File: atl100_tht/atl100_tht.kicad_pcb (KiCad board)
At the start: 2 copper layers, 150 x 100 mm, 43 parts, among them J1 Conn_01x04_Pin, J2 Screw_Terminal_01x02, J3 Screw_Terminal_01x02, J4 Screw_Terminal_01x02, J5 Screw_Terminal_01x02, J6 Screw_Terminal_01x04, J7 Screw_Terminal_01x04, J8 Screw_Terminal_01x06, U2 ESP32-S3 DevKit, U3 HW-519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

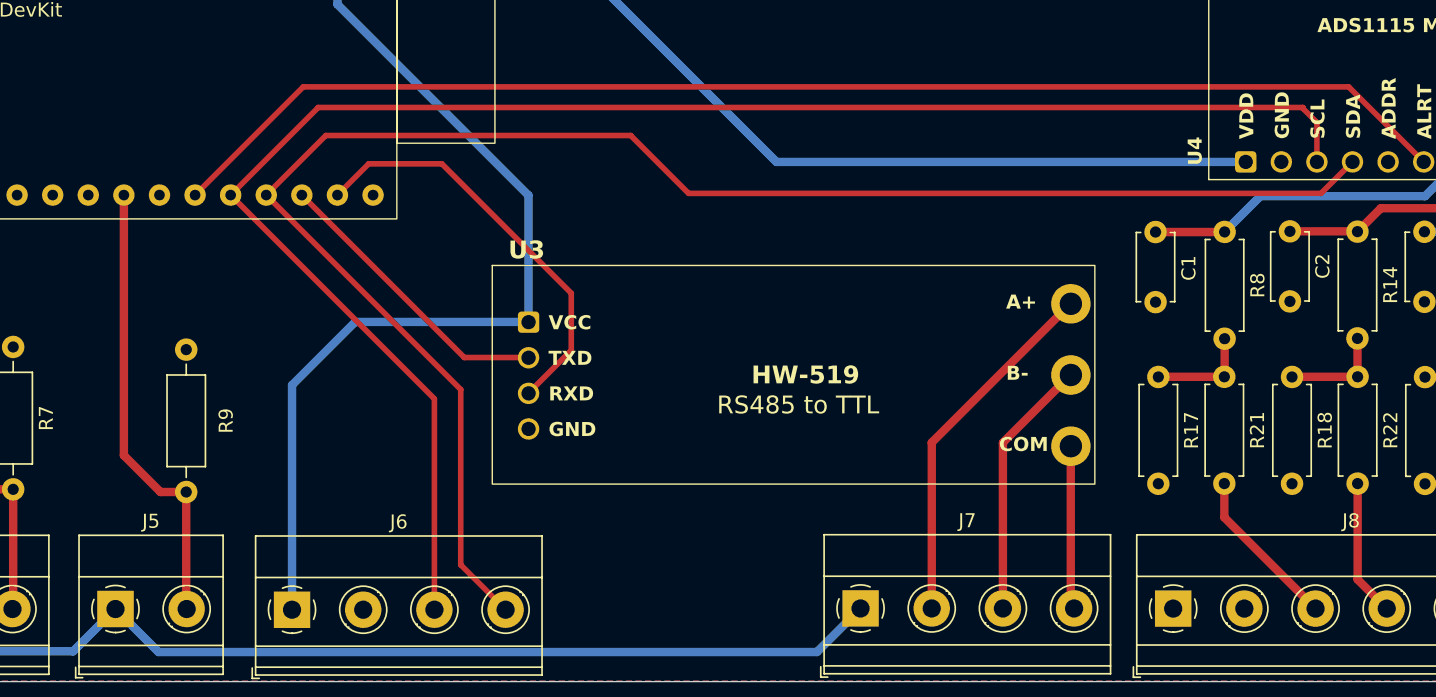
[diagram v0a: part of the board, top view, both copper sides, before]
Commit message: feat: Updated pins to RS-485 UART
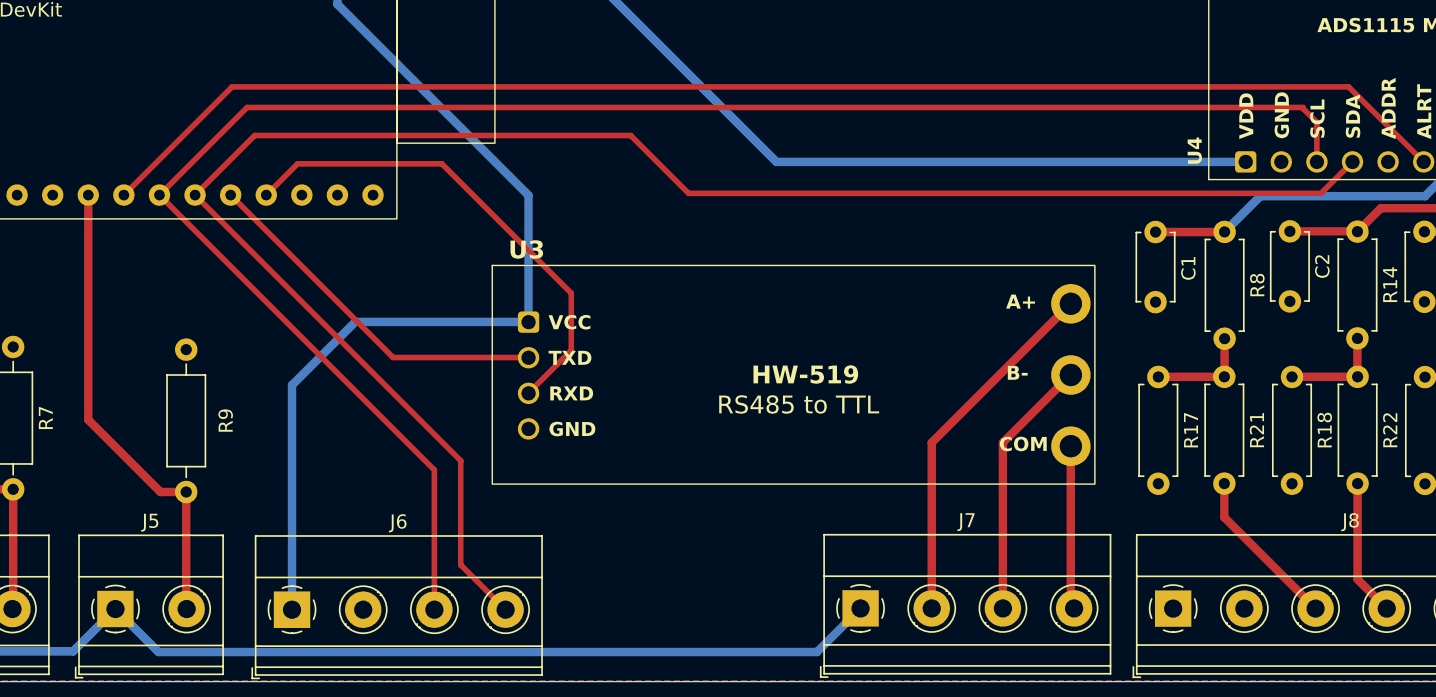
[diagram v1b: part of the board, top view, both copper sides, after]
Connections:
- U2 pad 24: MCU_TXD - RS485_RXD -> unconnected-(U2-U0TXD/GPIO43-Pad24)
- U2 pad 25: MCU_RXD - RS485_TXD -> unconnected-(U2-U0RXD/GPIO44-Pad25)
- U2 pad 26: I2C_SDA -> MCU_TXD - RS485_RXD
- U2 pad 27: I2C_SCL -> MCU_RXD - RS485_TXD
- U2 pad 28: ADC_ALERT -> I2C_SDA
- U2 pad 29: unconnected-(U2-MTDI/GPIO41-Pad29) -> I2C_SCL
- U2 pad 30: PL- -> ADC_ALERT
- U2 pad 31: unconnected-(U2-SUBSPICS1/MTCK/GPIO39-Pad31) -> PL-
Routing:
- net I2C_SDA: track 118.6 -> 125.8 mm
- net I2C_SCL: track 119.0 -> 126.2 mm
- net ADC_ALERT: track 93.1 -> 98.2 mm
- net MCU_RXD - RS485_TXD: track 21.0 -> 26.1 mm
- net MCU_TXD - RS485_RXD: track 29.8 -> 34.9 mm
- net PL-: track 32.5 -> 33.5 mm
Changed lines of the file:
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@@
 	(title_block
 		(title "ATL-100 (Multiparametric Station) - THT Based")
-		(date "2024-10-27")
+		(date "2024-10-29")
 		(rev "v1.0.0")
 		(company "AgroTechLab (Laboratório de Desenvolvimento de Tecnologias para o Agronegócio)")
@@
 	(net 19 "MCU_RXD - RS485_TXD")
 	(net 20 "ADC_ALERT")
-	(net 21 "unconnected-(U2-MTDI{slash}GPIO41-Pad29)")
+	(net 21 "unconnected-(U2-U0TXD{slash}GPIO43-Pad24)")
 	(net 22 "unconnected-(U2-SUBSPICLK{slash}FSPICLK{slash}SPIIO7{slash}GPIO36-Pad34)")
 	(net 23 "Net-(U4-A0)")
@@
 	(net 32 "unconnected-(U2-GPIO8{slash}RTC_GPIO8{slash}ADC1_CH7{slash}SUBSPICS1-Pad12)")
 	(net 33 "unconnected-(U2-RGB_LED{slash}SUBSPIWP{slash}FSPIWP{slash}GPIO38-Pad32)")
-	(net 34 "unconnected-(U2-SUBSPICS1{slash}MTCK{slash}GPIO39-Pad31)")
+	(net 34 "unconnected-(U2-U0RXD{slash}GPIO44-Pad25)")
 	(net 35 "unconnected-(U2-GPIO10{slash}RTC_GPIO10{slash}ADC1_CH9{slash}FSPICS0{slash}FSPIIO4{slash}SUBSPICS0-Pad16)")
 	(net 36 "unconnected-(U2-GPIO16{slash}RTC_GPIO16{slash}ADC2_CH5{slash}U0CTS-Pad9)")
@@
 		(tags "Resistor Axial_DIN0207 series Axial Horizontal pin pitch 10.16mm 0.25W = 1/4W length 6.3mm diameter 2.5mm")
 		(property "Reference" "R2"
-			(at 5.08 -2.37 360)
+			(at 5.08 -2.37 0)
 			(layer "F.SilkS")
 			(effects
@@
 		)
 		(property "Value" "42R"
-			(at 5.08 2.37 360)
+			(at 5.08 2.37 0)
 			(layer "F.Fab")
 			(effects
@@
 		)
 		(fp_text user "${REFERENCE}"
-			(at 5.08 0 360)
+			(at 5.08 0 0)
 			(layer "F.Fab")
 			(effects
@@
 			(layers "*.Cu" "*.Mask")
 			(remove_unused_layers no)
-			(net 18 "MCU_TXD - RS485_RXD")
+			(net 21 "unconnected-(U2-U0TXD{slash}GPIO43-Pad24)")
 			(pinfunction "U0TXD/GPIO43")
-			(pintype "bidirectional")
+			(pintype "bidirectional+no_connect")
 		)
 		(pad "25" thru_hole circle
@@
 			(layers "*.Cu" "*.Mask")
 			(remove_unused_layers no)
-			(net 19 "MCU_RXD - RS485_TXD")
+			(net 34 "unconnected-(U2-U0RXD{slash}GPIO44-Pad25)")
 			(pinfunction "U0RXD/GPIO44")
-			(pintype "bidirectional")
+			(pintype "bidirectional+no_connect")
 		)
 		(pad "26" thru_hole circle
@@
 			(layers "*.Cu" "*.Mask")
 			(remove_unused_layers no)
-			(net 10 "I2C_SDA")
+			(net 18 "MCU_TXD - RS485_RXD")
 			(pinfunction "ADC1_CH0/RTC_GPIO1/GPIO1")
 			(pintype "bidirectional")
@@
 			(layers "*.Cu" "*.Mask")
 			(remove_unused_layers no)
-			(net 12 "I2C_SCL")
+			(net 19 "MCU_RXD - RS485_TXD")
 			(pinfunction "ADC1_CH1/RTC_GPIO2/GPIO2")
 			(pintype "bidirectional")
@@
 			(layers "*.Cu" "*.Mask")
 			(remove_unused_layers no)
-			(net 20 "ADC_ALERT")
+			(net 10 "I2C_SDA")
 			(pinfunction "MTMS/GPIO42")
 			(pintype "bidirectional")
@@
 			(layers "*.Cu" "*.Mask")
 			(remove_unused_layers no)
-			(net 21 "unconnected-(U2-MTDI{slash}GPIO41-Pad29)")
+			(net 12 "I2C_SCL")
 			(pinfunction "MTDI/GPIO41")
-			(pintype "bidirectional+no_connect")
+			(pintype "bidirectional")
 		)
 		(pad "30" thru_hole circle
@@
 			(layers "*.Cu" "*.Mask")
 			(remove_unused_layers no)
-			(net 13 "PL-")
+			(net 20 "ADC_ALERT")
 			(pinfunction "MTDO/GPIO40")
 			(pintype "bidirectional")
@@
 			(layers "*.Cu" "*.Mask")
 			(remove_unused_layers no)
-			(net 34 "unconnected-(U2-SUBSPICS1{slash}MTCK{slash}GPIO39-Pad31)")
+			(net 13 "PL-")
 			(pinfunction "SUBSPICS1/MTCK/GPIO39")
-			(pintype "bidirectional+no_connect")
+			(pintype "bidirectional")
 		)
 		(pad "32" thru_hole circle
@@
 		(tags "THT Terminal Block Phoenix MKDS-1,5-6-5.08 pitch 5.08mm size 30.5x9.8mm^2 drill 1.3mm pad 2.6mm")
 		(property "Reference" "J8"
-			(at 12.7 -6.26 360)
+			(at 12.7 -6.26 0)
 			(layer "F.SilkS")
 			(effects
@@
 		)
 		(property "Value" "Screw_Terminal_01x06"
-			(at 12.7 5.66 360)
+			(at 12.7 5.66 0)
 			(layer "F.Fab")
 			(effects
@@
 		)
 		(fp_text user "${REFERENCE}"
-			(at 12.7 3.2 360)
+			(at 12.7 3.2 0)
 			(layer "F.Fab")
 			(effects
@@
 	)
 	(segment
-		(start 194.892 112.43)
-		(end 197.1372 110.1848)
+		(start 118.79 108.3)
+		(end 145.63 108.3)
 		(width 0.4)
 		(layer "F.Cu")
@@
 	)
 	(segment
-		(start 133.5 126.43)
-		(end 133.5 138.94)
+		(start 194.892 112.43)
+		(end 197.1372 110.1848)
 		(width 0.4)
 		(layer "F.Cu")
@@
 	)
 	(segment
-		(start 149.76 112.43)
-		(end 194.892 112.43)
+		(start 145.63 108.3)
+		(end 149.76 112.43)
 		(width 0.4)
 		(layer "F.Cu")
@@
 	)
 	(segment
-		(start 119.62 112.55)
-		(end 133.5 126.43)
+		(start 114.54 112.55)
+		(end 118.79 108.3)
 		(width 0.4)
 		(layer "F.Cu")
@@
 	)
 	(segment
-		(start 119.62 112.55)
-		(end 123.87 108.3)
+		(start 133.5 131.51)
+		(end 133.5 138.94)
 		(width 0.4)
 		(layer "F.Cu")
@@
 	)
 	(segment
-		(start 123.87 108.3)
-		(end 145.63 108.3)
+		(start 114.54 112.55)
+		(end 133.5 131.51)
 		(width 0.4)
 		(layer "F.Cu")
@@
 	)
 	(segment
-		(start 145.63 108.3)
-		(end 149.76 112.43)
+		(start 149.76 112.43)
+		(end 194.892 112.43)
 		(width 0.4)
 		(layer "F.Cu")
@@
 	)
 	(segment
-		(start 131.62 127.09)
-		(end 117.08 112.55)
+		(start 193.6 106.37)
+		(end 194.5972 107.3672)
 		(width 0.4)
 		(layer "F.Cu")
@@
 	)
 	(segment
-		(start 193.6 106.3)
-		(end 193.6 106.37)
+		(start 131.62 132.17)
+		(end 112 112.55)
 		(width 0.4)
 		(layer "F.Cu")
@@
 	)
 	(segment
-		(start 193.6 106.37)
-		(end 194.5972 107.3672)
+		(start 193.6 106.3)
+		(end 193.6 106.37)
 		(width 0.4)
 		(layer "F.Cu")
@@
 	(segment
 		(start 131.62 142.14)
-		(end 131.62 127.09)
+		(end 131.62 132.17)
 		(width 0.4)
 		(layer "F.Cu")
@@
 	)
 	(segment
-		(start 117.08 112.55)
-		(end 123.33 106.3)
+		(start 112 112.55)
+		(end 118.25 106.3)
 		(width 0.4)
 		(layer "F.Cu")
@@
 	)
 	(segment
-		(start 123.33 106.3)
+		(start 118.25 106.3)
 		(end 193.6 106.3)
 		(width 0.4)
@@
 	)
 	(segment
-		(start 113.91 133.74)
-		(end 113.91 142.06)
+		(start 112.07 133.74)
+		(end 106.92 128.59)
 		(width 0.6)
 		(layer "F.Cu")
@@
 	)
 	(segment
-		(start 109.46 131.13)
-		(end 109.46 112.55)
+		(start 113.91 133.74)
+		(end 113.91 142.06)
 		(width 0.6)
 		(layer "F.Cu")
@@
 	)
 	(segment
-		(start 113.91 133.74)
-		(end 112.07 133.74)
+		(start 106.92 128.59)
+		(end 106.92 112.55)
 		(width 0.6)
 		(layer "F.Cu")
@@
 	)
 	(segment
-		(start 112.07 133.74)
-		(end 109.46 131.13)
+		(start 113.91 133.74)
+		(end 112.07 133.74)
 		(width 0.6)
 		(layer "F.Cu")
@@
 	)
 	(segment
-		(start 124.7 112.55)
-		(end 126.93 110.32)
+		(start 132.15 110.32)
+		(end 141.39 119.56)
 		(width 0.4)
 		(layer "F.Cu")
@@
 	)
 	(segment
-		(start 126.93 110.32)
-		(end 132.15 110.32)
+		(start 119.62 112.55)
+		(end 121.85 110.32)
 		(width 0.4)
 		(layer "F.Cu")
@@
 	)
 	(segment
-		(start 132.15 110.32)
-		(end 141.39 119.56)
+		(start 121.85 110.32)
+		(end 132.15 110.32)
 		(width 0.4)
 		(layer "F.Cu")
@@
 	)
 	(segment
-		(start 133.7536 124.1436)
-		(end 122.16 112.55)
+		(start 128.6736 124.1436)
+		(end 117.08 112.55)
 		(width 0.4)
 		(layer "F.Cu")
@@
 	(segment
 		(start 138.3314 124.1436)
-		(end 133.7536 124.1436)
+		(end 128.6736 124.1436)
 		(width 0.4)
 		(layer "F.Cu")
@@
 	)
 	(segment
-		(start 122.26 104.83)
-		(end 114.54 112.55)
+		(start 202.2172 110.1848)
+		(end 196.8624 104.83)
 		(width 0.4)
 		(layer "F.Cu")
@@
 	(segment
 		(start 196.8624 104.83)
-		(end 122.26 104.83)
+		(end 117.18 104.83)
 		(width 0.4)
 		(layer "F.Cu")
@@
 	)
 	(segment
-		(start 202.2172 110.1848)
-		(end 196.8624 104.83)
+		(start 117.18 104.83)
+		(end 109.46 112.55)
 		(width 0.4)
 		(layer "F.Cu")

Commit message: feat: Released v0.1.0 of THT project
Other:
- board text added: "ATL-100 v0.1.0"
- board text removed: "ATL-100 v1.0.0"
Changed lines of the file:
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@@
 		(layer "Edge.Cuts")
 	)
-	(gr_text "ATL-100 v1.0.0"
+	(gr_text "ATL-100 v0.1.0"
 		(at 135.11 55.53 0)
 		(layer "F.SilkS")
